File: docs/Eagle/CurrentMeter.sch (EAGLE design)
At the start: 10 parts

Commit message: schematics finalized
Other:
- moved on the sheet: ESP8266
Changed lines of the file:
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@@
 <?xml version="1.0" encoding="utf-8"?>
 <!DOCTYPE eagle SYSTEM "eagle.dtd">
-<eagle version="9.4.1">
+<eagle version="9.4.2">
 <drawing>
 <settings>
@@
 <attribute name="VALUE" x="87.122" y="31.75" size="1.778" layer="96" rot="R90"/>
 </instance>
-<instance part="ESP8266" gate="G$1" x="180.34" y="71.12" smashed="yes">
-<attribute name="NAME" x="167.64" y="81.28" size="1.778" layer="95"/>
-<attribute name="VALUE" x="167.64" y="55.88" size="1.778" layer="96"/>
+<instance part="ESP8266" gate="G$1" x="180.34" y="66.04" smashed="yes">
+<attribute name="NAME" x="167.64" y="76.2" size="1.778" layer="95"/>
+<attribute name="VALUE" x="167.64" y="50.8" size="1.778" layer="96"/>
 </instance>
 </instances>
@@
 <junction x="111.76" y="12.7"/>
 <wire x1="215.9" y1="12.7" x2="203.2" y2="12.7" width="0.1524" layer="91"/>
-<wire x1="203.2" y1="12.7" x2="203.2" y2="60.96" width="0.1524" layer="91"/>
+<wire x1="203.2" y1="12.7" x2="203.2" y2="55.88" width="0.1524" layer="91"/>
 <junction x="203.2" y="12.7"/>
 <pinref part="ESP8266" gate="G$1" pin="GND"/>
-<wire x1="203.2" y1="60.96" x2="195.58" y2="60.96" width="0.1524" layer="91"/>
-<wire x1="203.2" y1="60.96" x2="203.2" y2="63.5" width="0.1524" layer="91"/>
-<junction x="203.2" y="60.96"/>
+<wire x1="203.2" y1="55.88" x2="195.58" y2="55.88" width="0.1524" layer="91"/>
+<wire x1="203.2" y1="55.88" x2="203.2" y2="58.42" width="0.1524" layer="91"/>
+<junction x="203.2" y="55.88"/>
 <pinref part="ESP8266" gate="G$1" pin="GPIO15"/>
-<wire x1="203.2" y1="63.5" x2="195.58" y2="63.5" width="0.1524" layer="91"/>
+<wire x1="203.2" y1="58.42" x2="195.58" y2="58.42" width="0.1524" layer="91"/>
 </segment>
 </net>
@@
 <wire x1="114.3" y1="60.96" x2="114.3" y2="96.52" width="0.1524" layer="91"/>
 <wire x1="114.3" y1="96.52" x2="157.48" y2="96.52" width="0.1524" layer="91"/>
-<wire x1="157.48" y1="96.52" x2="157.48" y2="73.66" width="0.1524" layer="91"/>
+<wire x1="157.48" y1="96.52" x2="157.48" y2="68.58" width="0.1524" layer="91"/>
 <pinref part="ESP8266" gate="G$1" pin="VCC"/>
-<wire x1="157.48" y1="73.66" x2="157.48" y2="60.96" width="0.1524" layer="91"/>
-<wire x1="157.48" y1="60.96" x2="162.56" y2="60.96" width="0.1524" layer="91"/>
+<wire x1="157.48" y1="68.58" x2="157.48" y2="55.88" width="0.1524" layer="91"/>
+<wire x1="157.48" y1="55.88" x2="162.56" y2="55.88" width="0.1524" layer="91"/>
 <pinref part="ESP8266" gate="G$1" pin="CH_PD"/>
-<wire x1="162.56" y1="73.66" x2="157.48" y2="73.66" width="0.1524" layer="91"/>
-<junction x="157.48" y="73.66"/>
+<wire x1="162.56" y1="68.58" x2="157.48" y2="68.58" width="0.1524" layer="91"/>
+<junction x="157.48" y="68.58"/>
 </segment>
 </net>
@@
 <segment>
 <pinref part="B1" gate="G$1" pin="D2"/>
-<wire x1="142.24" y1="83.82" x2="144.78" y2="83.82" width="0.1524" layer="91"/>
-<wire x1="144.78" y1="83.82" x2="144.78" y2="88.9" width="0.1524" layer="91"/>
-<wire x1="144.78" y1="88.9" x2="203.2" y2="88.9" width="0.1524" layer="91"/>
-<wire x1="203.2" y1="88.9" x2="203.2" y2="76.2" width="0.1524" layer="91"/>
+<wire x1="144.78" y1="83.82" x2="142.24" y2="83.82" width="0.1524" layer="91"/>
+<wire x1="142.24" y1="83.82" x2="200.66" y2="83.82" width="0.1524" layer="91"/>
+<wire x1="200.66" y1="83.82" x2="200.66" y2="71.12" width="0.1524" layer="91"/>
 <pinref part="ESP8266" gate="G$1" pin="RX"/>
-<wire x1="203.2" y1="76.2" x2="195.58" y2="76.2" width="0.1524" layer="91"/>
+<wire x1="200.66" y1="71.12" x2="195.58" y2="71.12" width="0.1524" layer="91"/>
 </segment>
 </net>
@@
 <segment>
 <pinref part="B1" gate="G$1" pin="*D3"/>
-<wire x1="142.24" y1="81.28" x2="147.32" y2="81.28" width="0.1524" layer="91"/>
-<wire x1="147.32" y1="81.28" x2="147.32" y2="83.82" width="0.1524" layer="91"/>
-<wire x1="147.32" y1="83.82" x2="198.12" y2="83.82" width="0.1524" layer="91"/>
+<wire x1="142.24" y1="81.28" x2="198.12" y2="81.28" width="0.1524" layer="91"/>
 <pinref part="ESP8266" gate="G$1" pin="TX"/>
-<wire x1="198.12" y1="83.82" x2="198.12" y2="78.74" width="0.1524" layer="91"/>
-<wire x1="198.12" y1="78.74" x2="195.58" y2="78.74" width="0.1524" layer="91"/>
-</segment>
-</net>
+<wire x1="198.12" y1="81.28" x2="198.12" y2="73.66" width="0.1524" layer="91"/>
+<wire x1="198.12" y1="73.66" x2="195.58" y2="73.66" width="0.1524" layer="91"/>
+</segment>
+</net>

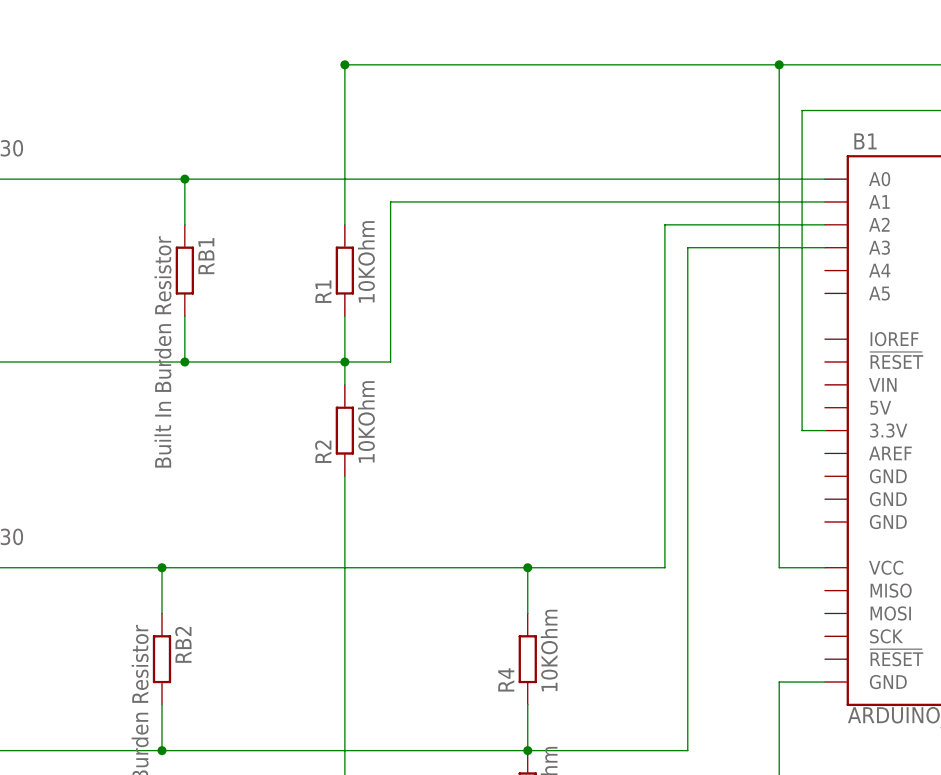
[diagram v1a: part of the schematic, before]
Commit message: Current meter schematic fix
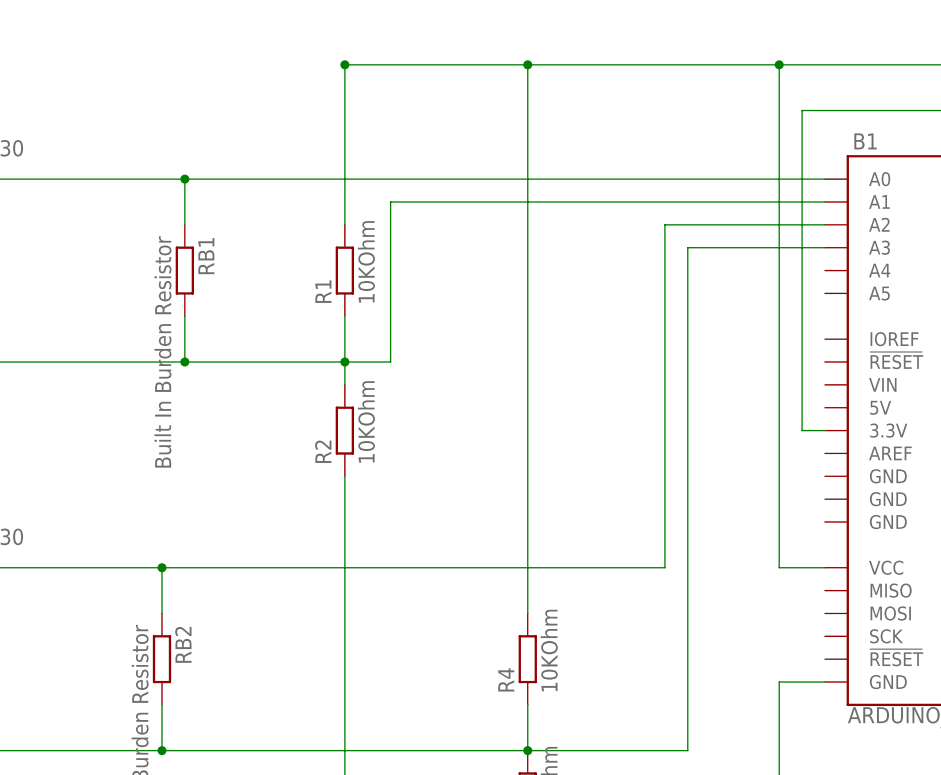
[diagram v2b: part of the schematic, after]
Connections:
- net N$3: now also R4.2
- net N$6: no longer R4.2
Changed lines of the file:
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@@
 <?xml version="1.0" encoding="utf-8"?>
 <!DOCTYPE eagle SYSTEM "eagle.dtd">
-<eagle version="9.4.2">
+<eagle version="9.4.1">
 <drawing>
 <settings>
@@
 <segment>
 <pinref part="R1" gate="G$1" pin="2"/>
-<wire x1="63.5" y1="101.6" x2="111.76" y2="101.6" width="0.1524" layer="91"/>
+<wire x1="63.5" y1="101.6" x2="83.82" y2="101.6" width="0.1524" layer="91"/>
+<wire x1="83.82" y1="101.6" x2="111.76" y2="101.6" width="0.1524" layer="91"/>
 <wire x1="111.76" y1="101.6" x2="215.9" y2="101.6" width="0.1524" layer="91"/>
 <wire x1="63.5" y1="83.82" x2="63.5" y2="101.6" width="0.1524" layer="91"/>
@@
 <pinref part="B1" gate="G$1" pin="VCC"/>
 <wire x1="111.76" y1="45.72" x2="116.84" y2="45.72" width="0.1524" layer="91"/>
+<pinref part="R4" gate="G$1" pin="2"/>
+<wire x1="83.82" y1="40.64" x2="83.82" y2="101.6" width="0.1524" layer="91"/>
+<junction x="83.82" y="101.6"/>
 </segment>
 </net>
@@
 <pinref part="YDHC_SCT-013-030" gate="G$1" pin="P$3"/>
 <wire x1="22.86" y1="45.72" x2="43.18" y2="45.72" width="0.1524" layer="91"/>
-<wire x1="43.18" y1="45.72" x2="83.82" y2="45.72" width="0.1524" layer="91"/>
-<wire x1="83.82" y1="45.72" x2="99.06" y2="45.72" width="0.1524" layer="91"/>
+<wire x1="43.18" y1="45.72" x2="99.06" y2="45.72" width="0.1524" layer="91"/>
 <wire x1="99.06" y1="45.72" x2="99.06" y2="83.82" width="0.1524" layer="91"/>
 <pinref part="B1" gate="G$1" pin="A2"/>
@@
 <wire x1="43.18" y1="40.64" x2="43.18" y2="45.72" width="0.1524" layer="91"/>
 <junction x="43.18" y="45.72"/>
-<pinref part="R4" gate="G$1" pin="2"/>
-<wire x1="83.82" y1="40.64" x2="83.82" y2="45.72" width="0.1524" layer="91"/>
-<junction x="83.82" y="45.72"/>
-</segment>
-</net>
+</segment>
+</net>

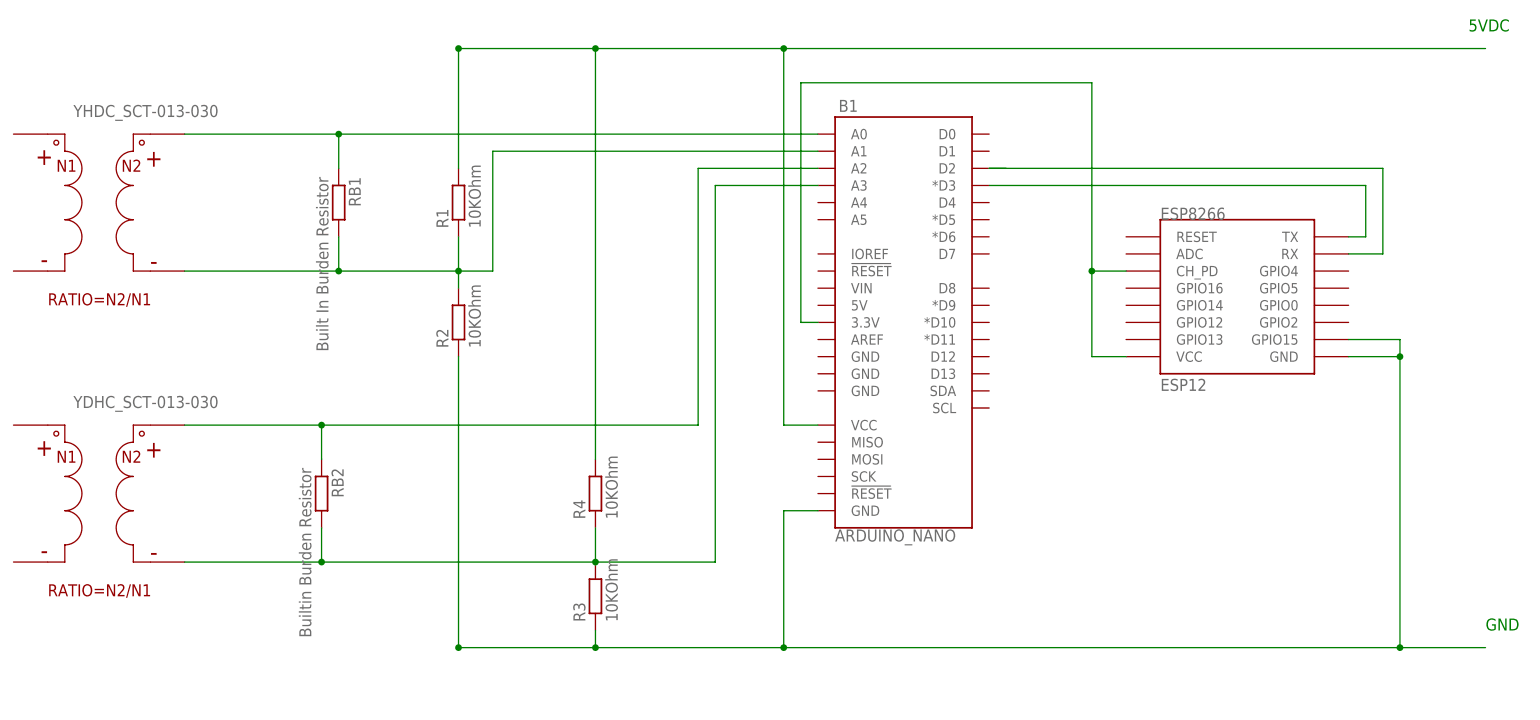
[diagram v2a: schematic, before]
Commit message: Documenting warm water pump
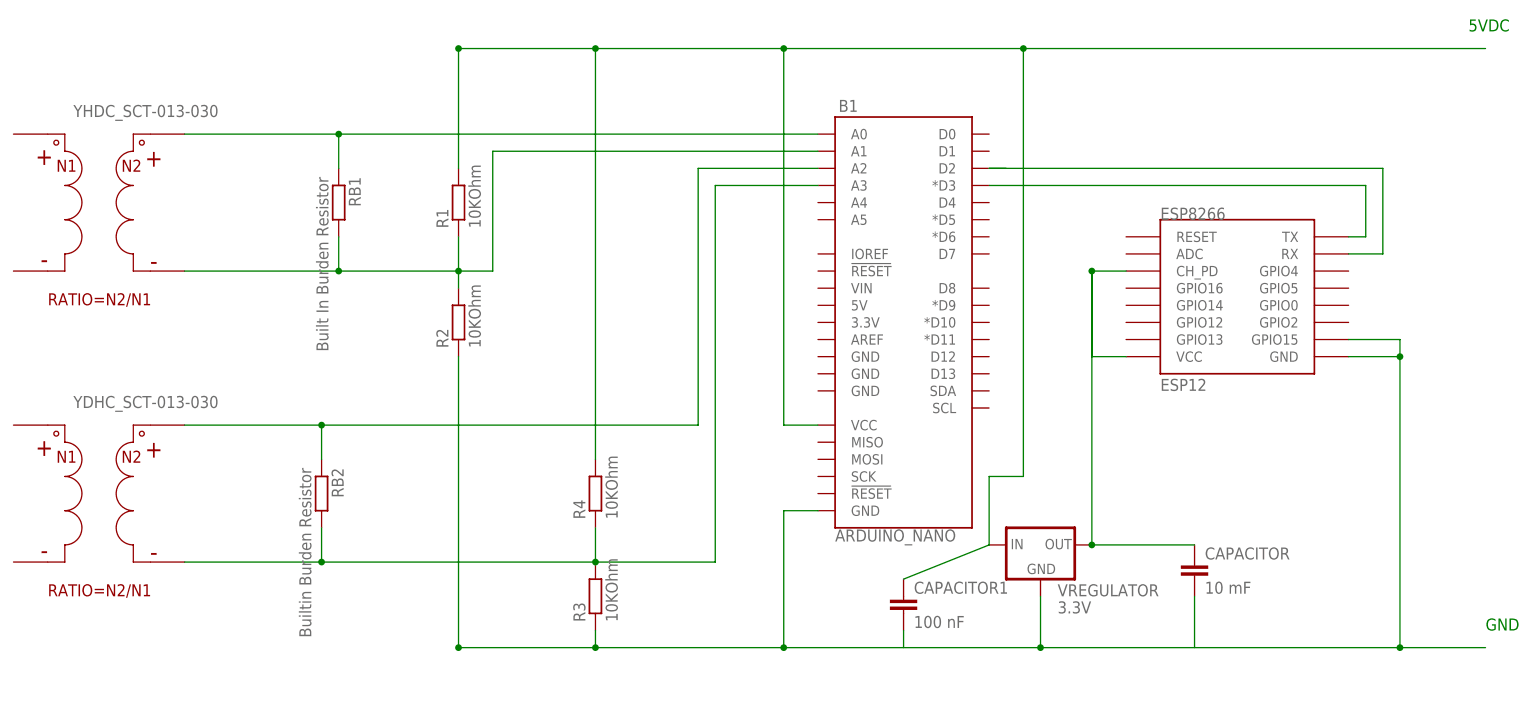
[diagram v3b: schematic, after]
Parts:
- added CAPACITOR: 10 mF, Nordic_nRF:CAPACITOR_0201_L
- added CAPACITOR1: 100 nF, Nordic_nRF:CAPACITOR_0201_L
- added VREGULATOR: 3.3V, DC_LOAD_AU:78LXX
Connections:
- new net N$19: CAPACITOR1.2
- new net N$9: CAPACITOR.2
- net N$3: now also CAPACITOR1.1, VREGULATOR.IN
- net N$4: now also VREGULATOR.GND
- net N$7: now also CAPACITOR.1, VREGULATOR.OUT; no longer B1.3.3V
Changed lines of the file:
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@@
 <layer number="115" name="ReferenceISLANDS" color="7" fill="1" visible="yes" active="yes"/>
 <layer number="116" name="Patch_BOT" color="9" fill="4" visible="yes" active="yes"/>
+<layer number="117" name="BACKMAAT1" color="7" fill="1" visible="yes" active="yes"/>
 <layer number="118" name="Rect_Pads" color="7" fill="1" visible="yes" active="yes"/>
+<layer number="119" name="KAP_TEKEN" color="7" fill="1" visible="yes" active="yes"/>
+<layer number="120" name="KAP_MAAT1" color="7" fill="1" visible="yes" active="yes"/>
 <layer number="121" name="_tsilk" color="7" fill="1" visible="yes" active="yes"/>
 <layer number="122" name="_bsilk" color="7" fill="1" visible="yes" active="yes"/>
@@
 <layer number="128" name="_bValues" color="7" fill="1" visible="yes" active="yes"/>
 <layer number="129" name="Mask" color="7" fill="1" visible="yes" active="yes"/>
+<layer number="130" name="SMDSTROOK" color="7" fill="1" visible="yes" active="yes"/>
 <layer number="131" name="tAdjust" color="7" fill="1" visible="yes" active="yes"/>
 <layer number="132" name="bAdjust" color="7" fill="1" visible="yes" active="yes"/>
+<layer number="133" name="bottom_silk" color="7" fill="1" visible="yes" active="yes"/>
 <layer number="144" name="Drill_legend" color="7" fill="1" visible="yes" active="yes"/>
 <layer number="150" name="Notes" color="7" fill="1" visible="yes" active="yes"/>
@@
 <layer number="230" name="230bmp" color="7" fill="1" visible="yes" active="yes"/>
 <layer number="231" name="231bmp" color="7" fill="1" visible="yes" active="yes"/>
+<layer number="232" name="Eagle3D_PG2" color="7" fill="1" visible="no" active="no"/>
+<layer number="233" name="Eagle3D_PG3" color="7" fill="1" visible="no" active="no"/>
 <layer number="248" name="Housing" color="7" fill="1" visible="yes" active="yes"/>
 <layer number="249" name="Edge" color="7" fill="1" visible="yes" active="yes"/>
@@
 <part name="R4" library="eagle-ltspice" library_urn="urn:adsk.eagle:library:217" deviceset="R" device="" package3d_urn="urn:adsk.eagle:package:13300/1" value="10KOhm"/>
 <part name="ESP8266" library="esp8266modules" deviceset="ESP12" device="" value="ESP12"/>
+<part name="VREGULATOR" library="DC_LOAD_AU" library_urn="urn:adsk.eagle:library:220454" deviceset="78LXX" device="" package3d_urn="urn:adsk.eagle:package:220577/2" value="3.3V"/>
+<part name="CAPACITOR1" library="Nordic_nRF" library_urn="urn:adsk.eagle:library:169009" deviceset="CAPACITOR" device="_0201_L" package3d_urn="urn:adsk.eagle:package:2593725/1" value="100 nF"/>
+<part name="CAPACITOR" library="Nordic_nRF" library_urn="urn:adsk.eagle:library:169009" deviceset="CAPACITOR" device="_0201_L" package3d_urn="urn:adsk.eagle:package:2593725/1" value="10 mF"/>
 </parts>
 <sheets>
@@
 <attribute name="NAME" x="167.64" y="76.2" size="1.778" layer="95"/>
 <attribute name="VALUE" x="167.64" y="50.8" size="1.778" layer="96"/>
+</instance>
+<instance part="VREGULATOR" gate="1" x="149.86" y="27.94" smashed="yes">
+<attribute name="NAME" x="152.4" y="20.32" size="1.778" layer="95"/>
+<attribute name="VALUE" x="152.4" y="17.78" size="1.778" layer="96"/>
+</instance>
+<instance part="CAPACITOR1" gate="C$1" x="129.54" y="20.32" smashed="yes">
+<attribute name="NAME" x="131.064" y="20.701" size="1.778" layer="95"/>
+<attribute name="VALUE" x="131.064" y="15.621" size="1.778" layer="96"/>
+</instance>
+<instance part="CAPACITOR" gate="C$1" x="172.72" y="25.4" smashed="yes">
+<attribute name="NAME" x="174.244" y="25.781" size="1.778" layer="95"/>
+<attribute name="VALUE" x="174.244" y="20.701" size="1.778" layer="96"/>
 </instance>
 </instances>
@@
 <wire x1="63.5" y1="101.6" x2="83.82" y2="101.6" width="0.1524" layer="91"/>
 <wire x1="83.82" y1="101.6" x2="111.76" y2="101.6" width="0.1524" layer="91"/>
-<wire x1="111.76" y1="101.6" x2="215.9" y2="101.6" width="0.1524" layer="91"/>
+<wire x1="111.76" y1="101.6" x2="147.32" y2="101.6" width="0.1524" layer="91"/>
+<wire x1="147.32" y1="101.6" x2="215.9" y2="101.6" width="0.1524" layer="91"/>
 <wire x1="63.5" y1="83.82" x2="63.5" y2="101.6" width="0.1524" layer="91"/>
 <junction x="63.5" y="101.6"/>
@@
 <wire x1="83.82" y1="40.64" x2="83.82" y2="101.6" width="0.1524" layer="91"/>
 <junction x="83.82" y="101.6"/>
+<pinref part="VREGULATOR" gate="1" pin="IN"/>
+<wire x1="142.24" y1="27.94" x2="142.24" y2="38.1" width="0.1524" layer="91"/>
+<wire x1="142.24" y1="38.1" x2="147.32" y2="38.1" width="0.1524" layer="91"/>
+<wire x1="147.32" y1="38.1" x2="147.32" y2="101.6" width="0.1524" layer="91"/>
+<junction x="147.32" y="101.6"/>
+<pinref part="CAPACITOR1" gate="C$1" pin="1"/>
+<wire x1="142.24" y1="27.94" x2="129.54" y2="22.86" width="0.1524" layer="91"/>
 </segment>
 </net>
@@
 <wire x1="63.5" y1="12.7" x2="83.82" y2="12.7" width="0.1524" layer="91"/>
 <wire x1="83.82" y1="12.7" x2="111.76" y2="12.7" width="0.1524" layer="91"/>
-<wire x1="111.76" y1="12.7" x2="203.2" y2="12.7" width="0.1524" layer="91"/>
+<wire x1="111.76" y1="12.7" x2="149.86" y2="12.7" width="0.1524" layer="91"/>
+<wire x1="149.86" y1="12.7" x2="203.2" y2="12.7" width="0.1524" layer="91"/>
 <wire x1="63.5" y1="55.88" x2="63.5" y2="12.7" width="0.1524" layer="91"/>
 <junction x="63.5" y="12.7"/>
@@
 <pinref part="ESP8266" gate="G$1" pin="GPIO15"/>
 <wire x1="203.2" y1="58.42" x2="195.58" y2="58.42" width="0.1524" layer="91"/>
+<pinref part="VREGULATOR" gate="1" pin="GND"/>
+<wire x1="149.86" y1="20.32" x2="149.86" y2="12.7" width="0.1524" layer="91"/>
+<junction x="149.86" y="12.7"/>
 </segment>
 </net>
@@
 <net name="N$7" class="0">
 <segment>
-<pinref part="B1" gate="G$1" pin="3.3V"/>
-<wire x1="116.84" y1="60.96" x2="114.3" y2="60.96" width="0.1524" layer="91"/>
-<wire x1="114.3" y1="60.96" x2="114.3" y2="96.52" width="0.1524" layer="91"/>
-<wire x1="114.3" y1="96.52" x2="157.48" y2="96.52" width="0.1524" layer="91"/>
-<wire x1="157.48" y1="96.52" x2="157.48" y2="68.58" width="0.1524" layer="91"/>
+<wire x1="157.48" y1="27.94" x2="157.48" y2="68.58" width="0.1524" layer="91"/>
 <pinref part="ESP8266" gate="G$1" pin="VCC"/>
 <wire x1="157.48" y1="68.58" x2="157.48" y2="55.88" width="0.1524" layer="91"/>
@@
 <wire x1="162.56" y1="68.58" x2="157.48" y2="68.58" width="0.1524" layer="91"/>
 <junction x="157.48" y="68.58"/>
+<pinref part="VREGULATOR" gate="1" pin="OUT"/>
+<pinref part="CAPACITOR" gate="C$1" pin="1"/>
+<wire x1="172.72" y1="27.94" x2="157.48" y2="27.94" width="0.1524" layer="91"/>
+<junction x="157.48" y="27.94"/>
 </segment>
 </net>
@@
 </segment>
 </net>
+<net name="N$19" class="0">
+<segment>
+<pinref part="CAPACITOR1" gate="C$1" pin="2"/>
+<wire x1="129.54" y1="15.24" x2="129.54" y2="12.7" width="0.1524" layer="91"/>
+</segment>
+</net>
+<net name="N$9" class="0">
+<segment>
+<pinref part="CAPACITOR" gate="C$1" pin="2"/>
+<wire x1="172.72" y1="20.32" x2="172.72" y2="12.7" width="0.1524" layer="91"/>
+</segment>
+</net>
